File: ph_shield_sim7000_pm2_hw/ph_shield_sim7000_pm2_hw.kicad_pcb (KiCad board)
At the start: 2 copper layers, 70 x 70 mm, 86 parts, among them J1 Conn_01x04, J2 Conn_01x07, J3 Conn_01x04, J4 USB_OTG, J5 I2C, J6 Conn_01x10, J7 SIM_Card, Q1 C1815, Q2 C1815, Q3 C1815, Q4 C1815, U1 TXS0108EPW, U2 LM2596S-ADJ, U3 SIM7000E, U4 TVS_Diode_Array_SMF05C

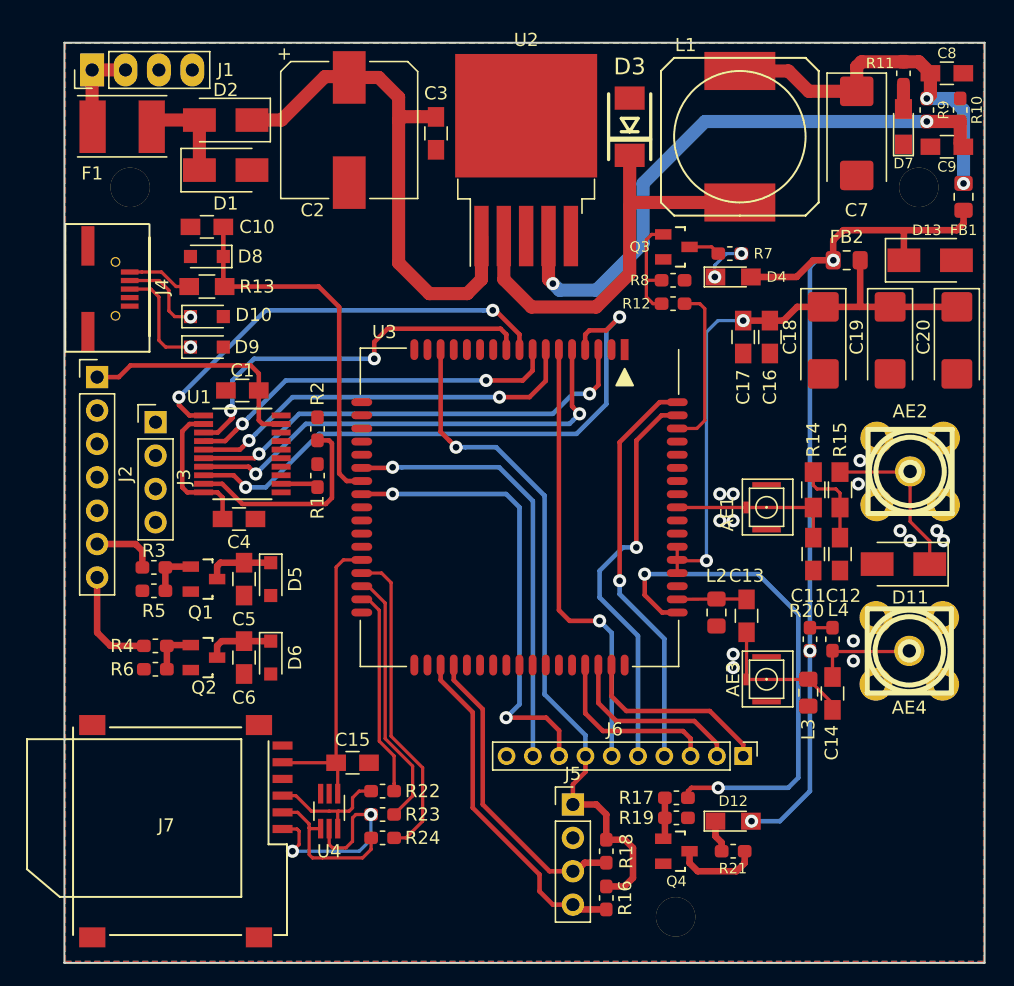
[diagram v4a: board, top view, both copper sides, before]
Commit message: Board SIM7000E is finished
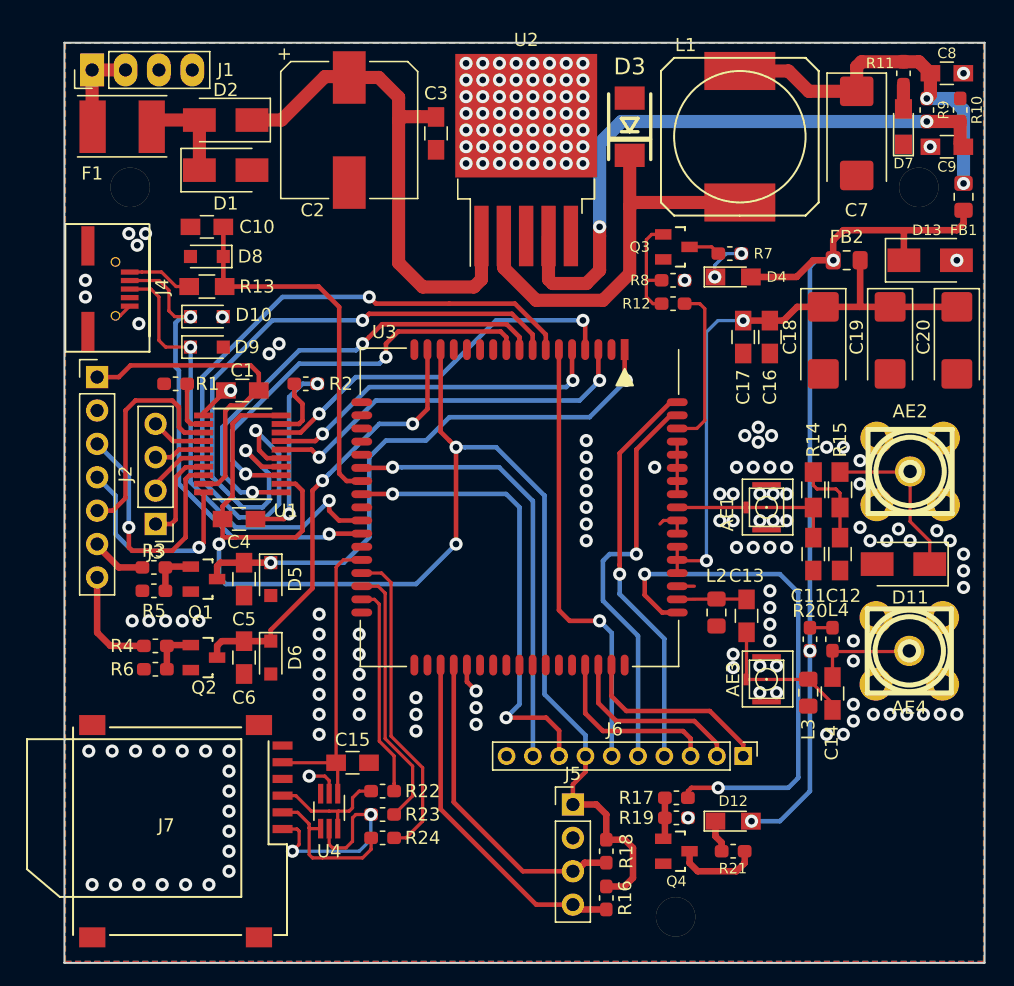
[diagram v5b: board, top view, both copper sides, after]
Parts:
- moved R1 12.9 mm to (108.5, 75.9), turned to 180 degrees
- moved J3 7.75 mm to (106.9, 86.6), turned to 180 degrees
- moved R2 3.54 mm to (118.4, 75.9), turned to 180 degrees
- turned U1 to 180 degrees
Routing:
- net /VDD_EXT: track 64.1 -> 107.1 mm, vias 1 -> 3
- net Net-(C5-Pad1): track 5.18 -> 43.9 mm, vias 0 -> 2
- net GND: track 0.00 -> 30.8 mm, vias 14 -> 182
- net /USB_DM: track 6.72 -> 36.1 mm, vias 1 -> 2
- net Net-(C6-Pad1): track 5.13 -> 33.7 mm, vias 0 -> 2
- net /USB_DP: track 8.41 -> 35.0 mm, vias 1 -> 2
- net /UART_CTS: track 30.6 -> 56.1 mm
- net /UART_RTS: track 28.9 -> 48.9 mm
- net /3V3_RX: track 0.00 -> 19.6 mm, vias 0 -> 1
- net /3V3_RI: track 0.00 -> 17.4 mm
- net /3V3_TX: track 0.00 -> 16.2 mm, vias 0 -> 1
- net /UART_RI: track 45.0 -> 28.8 mm
- net Net-(R2-Pad2): track 15.9 -> 4.78 mm
- net /UART_DCD: track 35.9 -> 26.5 mm
- net /3V3_RTS: track 0.00 -> 7.35 mm
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
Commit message: door_fume_hood
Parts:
- added G***: LOGO, PH_Footprint:logo, B.Cu at (161.0, 115.0)
- added G***: LOGO, PH_Footprint:logo, F.Cu at (161.0, 115.0)
- AE3: value Antenna -> Antenna_Shield
- J2, J3: moved to B.Cu
- turned J2 to 180 degrees
- turned J3 to 0 degrees
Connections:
- AE3 pad 2: (no net) -> GND
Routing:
- net GND: vias 182 -> 166
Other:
- board text added: "+3V3"
- board text added: "ADC"
- board text added: "CFG"
- board text added: "CTS"
- board text added: "DCD"
- board text added: "DTR"
- board text added: "GND"
- board text added: "GPIO2"
- board text added: "GPIO3"
- board text added: "GPIO4"
- board text added: "PWR"
- board text added: "RI"
- board text added: "RST"
- board text added: "RTS"
- board text added: "RX"
- board text added: "RX3"
- board text added: "SCL"
- board text added: "SDA"
- board text added: "SIM7000E"
- board text added: "TX"
- board text added: "TX3"
- board text added: "VDD"
